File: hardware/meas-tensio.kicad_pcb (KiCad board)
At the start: 2 copper layers, 77.5 x 47 mm, 44 parts, among them J1 Tens4, J2 Tens3, J3 Tens2, J4 Tens1, J6 CAN1, J7 CAN2, P1 CONN_PROG+SER_AVR, Q1 BSS83P, U1 ATMEGA168PA-AU, U2 MCP2515-E/SO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

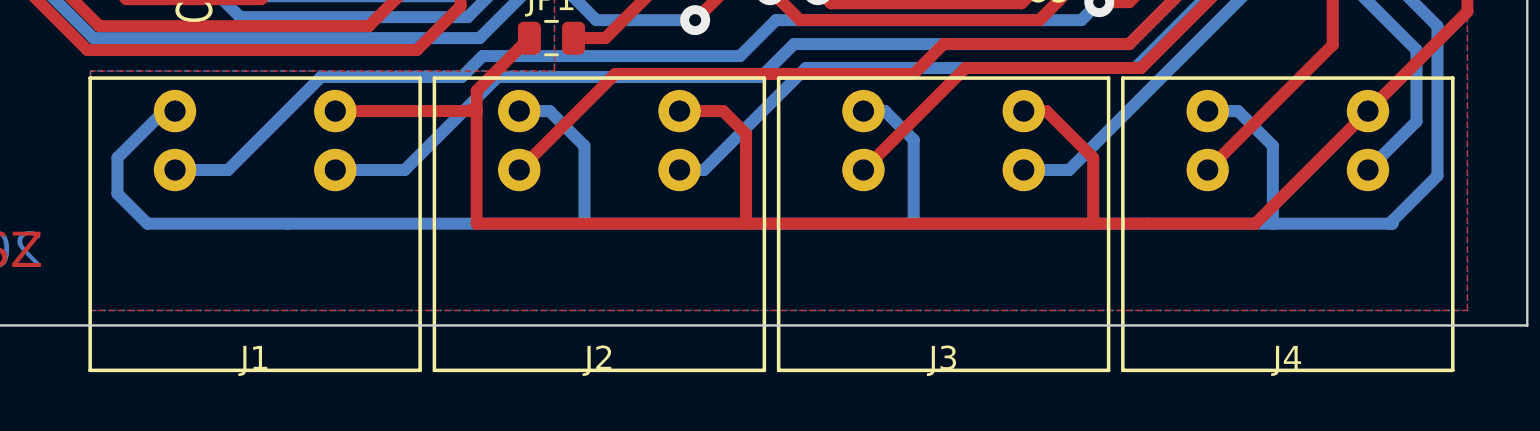
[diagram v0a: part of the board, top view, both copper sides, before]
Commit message: Connect screen of Mini-DIN plug to GND
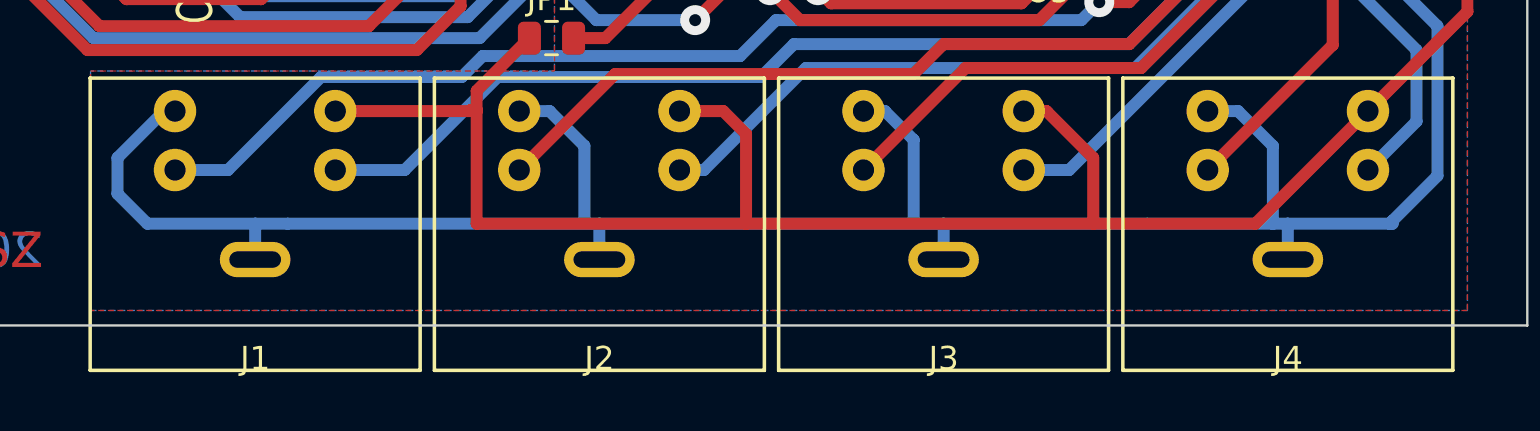
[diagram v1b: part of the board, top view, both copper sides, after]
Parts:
- C10, C9: value 22p -> 33p
- C3: value 0.1µ -> 100n
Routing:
- net GNDA: track 324.9 -> 330.9 mm

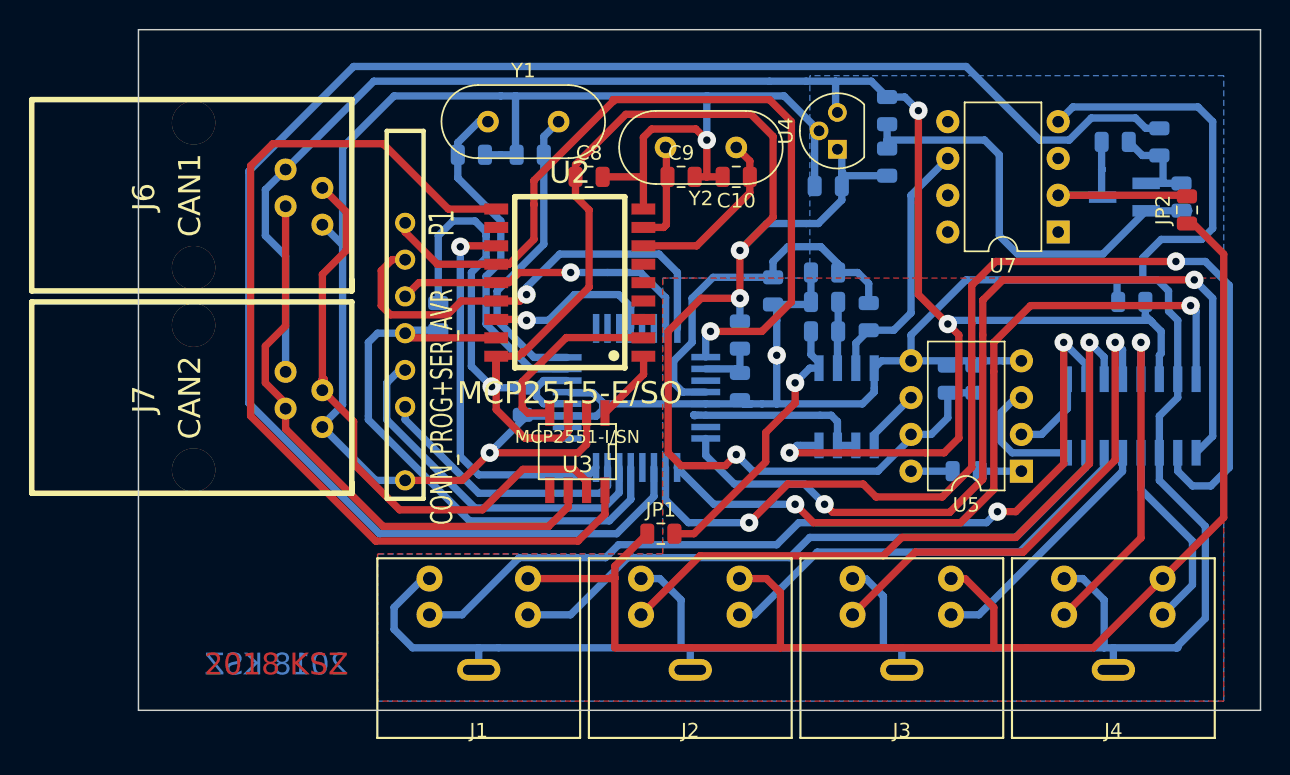
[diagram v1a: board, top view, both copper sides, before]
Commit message: Fix conflicting capacitor placement
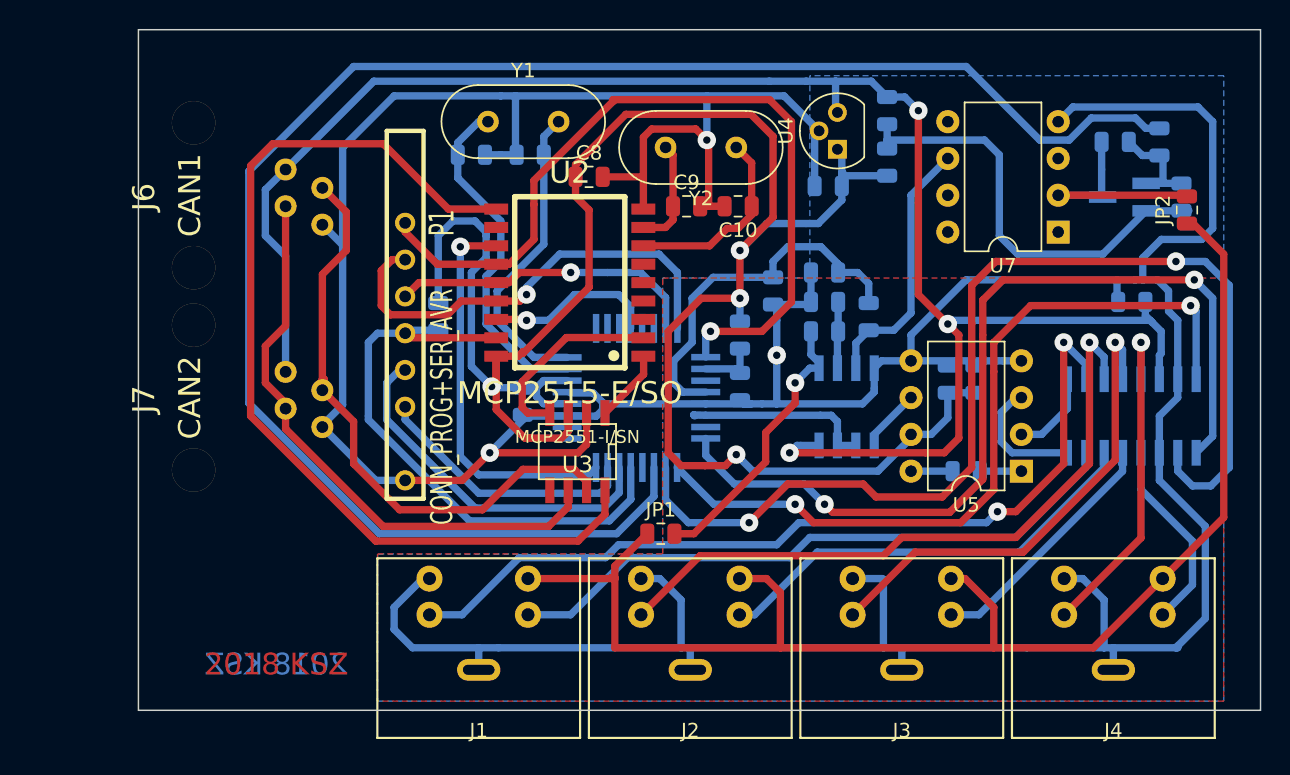
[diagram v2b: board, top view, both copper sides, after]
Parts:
- moved C9 2.07 mm to (241.0, 124.0)
- moved C10 2.04 mm to (244.6, 124.0)
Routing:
- net GNDA: track 330.9 -> 333.4 mm
- net Net-(C10-Pad1): track 12.4 -> 13.5 mm

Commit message: Remove unnecessary jumper. Remove ground loop.
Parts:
- removed JP1: a10, Resistor_SMD:R_0805_2012Metric
- removed JP2: ad, Resistor_SMD:R_0805_2012Metric
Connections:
- R2 pad 1: Net-(JP1-Pad2) -> Net-(J1-Pad3)
- U6 pad 1: Net-(JP1-Pad2) -> Net-(J1-Pad3)
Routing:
- net Net-(JP1-Pad2): track 19.5 -> 0.00 mm, vias 1 -> 0
- net Net-(C3-Pad1): track 15.9 -> 6.96 mm
- net Net-(J1-Pad3): track 96.3 -> 90.1 mm, vias 0 -> 1
